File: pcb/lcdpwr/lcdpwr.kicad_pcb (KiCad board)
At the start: 2 copper layers, 63.4 x 37.8 mm, 29 parts, among them J1 CONN_01X03, J2 CONN_01X03, J3 CONN_01X03, J4 TEST_1P, J5 CONN_02X13, J6 TEST_1P, J7 CONN_01X03, J8 TEST_1P, U1 LT3463, U2 MC33063A

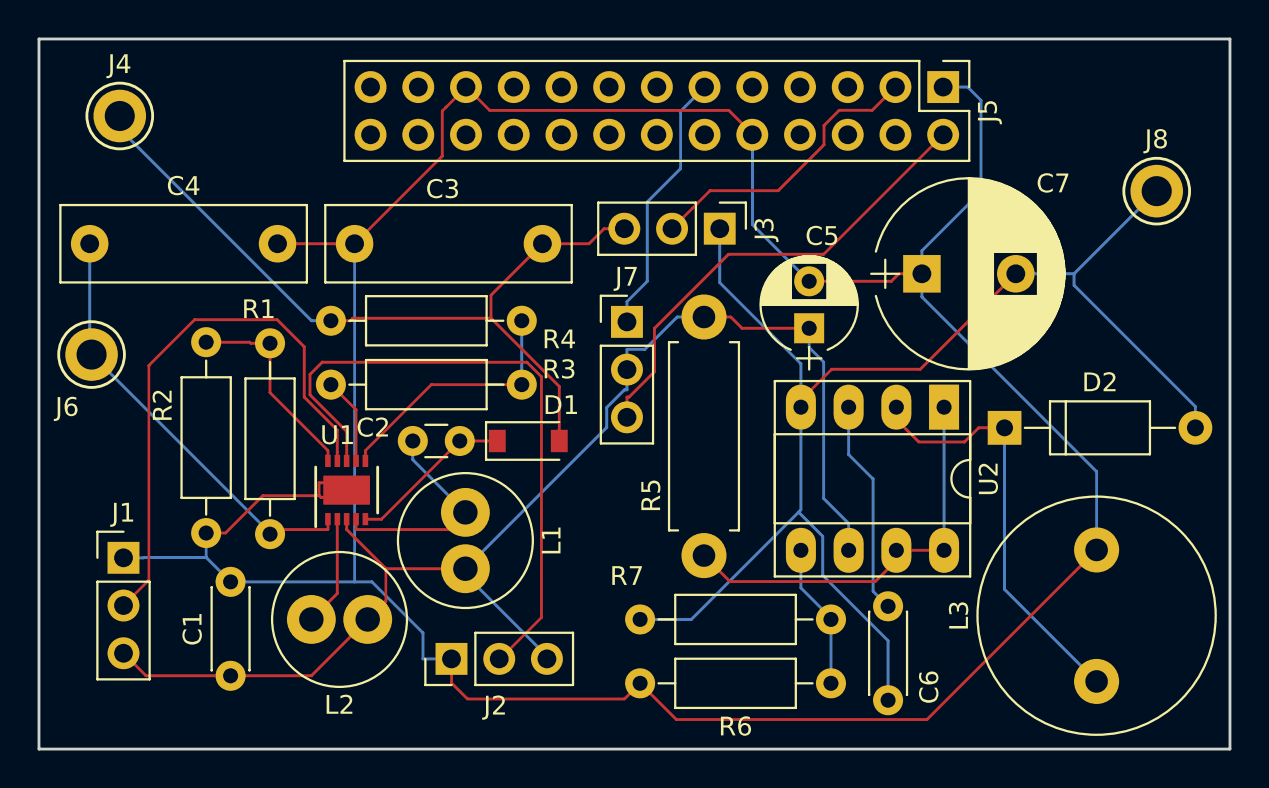
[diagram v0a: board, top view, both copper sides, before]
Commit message: Migrate other PCBs from KiCad 4 to KiCad 8
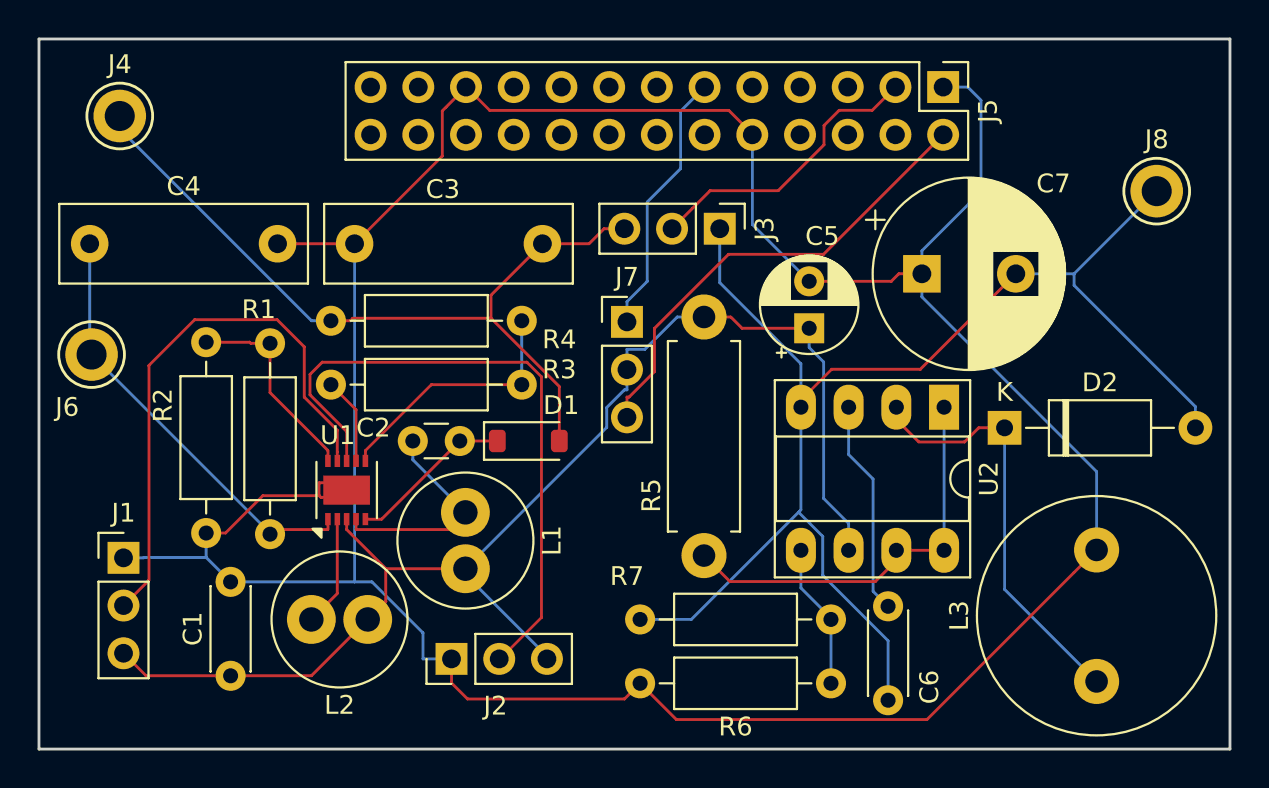
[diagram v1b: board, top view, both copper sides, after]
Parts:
- C1, C6: footprint Capacitors_THT:C_Disc_D4.3mm_W1.9mm_P5.00mm -> Capacitor_THT:C_Disc_D4.3mm_W1.9mm_P5.00mm
- C2: footprint Capacitors_THT:C_Disc_D3.0mm_W1.6mm_P2.50mm -> Capacitor_THT:C_Disc_D3.0mm_W1.6mm_P2.50mm
- C3, C4: footprint Capacitors_THT:C_Rect_L13.0mm_W4.0mm_P10.00mm_FKS3_FKP3_MKS4 -> Capacitor_THT:C_Rect_L13.0mm_W4.0mm_P10.00mm_FKS3_FKP3_MKS4
- C5: footprint Capacitors_THT:CP_Radial_D5.0mm_P2.50mm -> Capacitor_THT:CP_Radial_D5.0mm_P2.50mm
- C7: footprint Capacitors_THT:CP_Radial_D10.0mm_P5.00mm -> Capacitor_THT:CP_Radial_D10.0mm_P5.00mm
- D1: footprint Diodes_SMD:D_SOD-123 -> Diode_SMD:D_SOD-123
- D2: footprint Diodes_THT:D_A-405_P10.16mm_Horizontal -> Diode_THT:D_A-405_P10.16mm_Horizontal
- J1, J2, J3, J7: value CONN_01X03 -> Conn_01x03; footprint Pin_Headers:Pin_Header_Straight_1x03_Pitch2.54mm -> Connector_PinHeader_2.54mm:PinHeader_1x03_P2.54mm_Vertical
- J4, J6, J8: value TEST_1P -> TestPoint; footprint Measurement_Points:Test_Point_Keystone_5010-5014_Multipurpose -> TestPoint:TestPoint_Keystone_5010-5014_Multipurpose
- J5: value CONN_02X13 -> Conn_02x13_Odd_Even; footprint Pin_Headers:Pin_Header_Straight_2x13_Pitch2.54mm -> Connector_PinHeader_2.54mm:PinHeader_2x13_P2.54mm_Vertical
- L1, L2: footprint Inductors_THT:L_Radial_D7.0mm_P3.00mm -> Inductor_THT:L_Radial_D7.0mm_P3.00mm
- L3: footprint Inductors_THT:L_Radial_D12.5mm_P7.00mm_Fastron_09HCP -> Inductor_THT:L_Radial_D12.5mm_P7.00mm_Fastron_09HCP
- R1, R2, R3, R4, R6, R7: footprint Resistors_THT:R_Axial_DIN0207_L6.3mm_D2.5mm_P10.16mm_Horizontal -> Resistor_THT:R_Axial_DIN0207_L6.3mm_D2.5mm_P10.16mm_Horizontal
- R5: footprint Resistors_THT:R_Axial_DIN0411_L9.9mm_D3.6mm_P12.70mm_Horizontal -> Resistor_THT:R_Axial_DIN0411_L9.9mm_D3.6mm_P12.70mm_Horizontal
- U1: footprint Housings_DFN_QFN:DFN-10-1EP_3x3mm_Pitch0.5mm -> Package_DFN_QFN:DFN-10-1EP_3x3mm_P0.5mm_EP1.55x2.48mm
- U2: footprint Housings_DIP:DIP-8_W7.62mm_Socket_LongPads -> Package_DIP:DIP-8_W7.62mm_Socket_LongPads
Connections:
- J5 pad 12: Net-(J5-Pad12) -> unconnected-(J5-Pin_12-Pad12)
- J5 pad 13: Net-(J5-Pad13) -> unconnected-(J5-Pin_13-Pad13)
- J5 pad 14: Net-(J5-Pad14) -> unconnected-(J5-Pin_14-Pad14)
- J5 pad 15: Net-(J5-Pad15) -> unconnected-(J5-Pin_15-Pad15)
- J5 pad 16: Net-(J5-Pad16) -> unconnected-(J5-Pin_16-Pad16)
- J5 pad 17: Net-(J5-Pad17) -> unconnected-(J5-Pin_17-Pad17)
- J5 pad 18: Net-(J5-Pad18) -> unconnected-(J5-Pin_18-Pad18)
- J5 pad 19: Net-(J5-Pad19) -> unconnected-(J5-Pin_19-Pad19)
- J5 pad 20: Net-(J5-Pad20) -> unconnected-(J5-Pin_20-Pad20)
- J5 pad 22: Net-(J5-Pad22) -> unconnected-(J5-Pin_22-Pad22)
- J5 pad 23: Net-(J5-Pad23) -> unconnected-(J5-Pin_23-Pad23)
- J5 pad 24: Net-(J5-Pad24) -> unconnected-(J5-Pin_24-Pad24)
- J5 pad 25: Net-(J5-Pad25) -> unconnected-(J5-Pin_25-Pad25)
- J5 pad 26: Net-(J5-Pad26) -> unconnected-(J5-Pin_26-Pad26)
- J5 pad 4: Net-(J5-Pad4) -> unconnected-(J5-Pin_4-Pad4)
- J5 pad 5: Net-(J5-Pad5) -> unconnected-(J5-Pin_5-Pad5)
- J5 pad 6: Net-(J5-Pad6) -> unconnected-(J5-Pin_6-Pad6)
- J5 pad 7: Net-(J5-Pad7) -> unconnected-(J5-Pin_7-Pad7)
- J5 pad 8: Net-(J5-Pad8) -> unconnected-(J5-Pin_8-Pad8)
- J5 pad 9: Net-(J5-Pad9) -> unconnected-(J5-Pin_9-Pad9)
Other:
- net class Default removed
